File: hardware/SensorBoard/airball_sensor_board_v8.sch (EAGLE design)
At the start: 61 parts, among them IC1 CP2102, J2 USB Female Type C Connector, T1 BC846, T2 BC846, U1 BQ24075, U2 BQ27441-G1, U3 BMP388, U4 ESP-WROOM-32, U7 SP0503BAHT

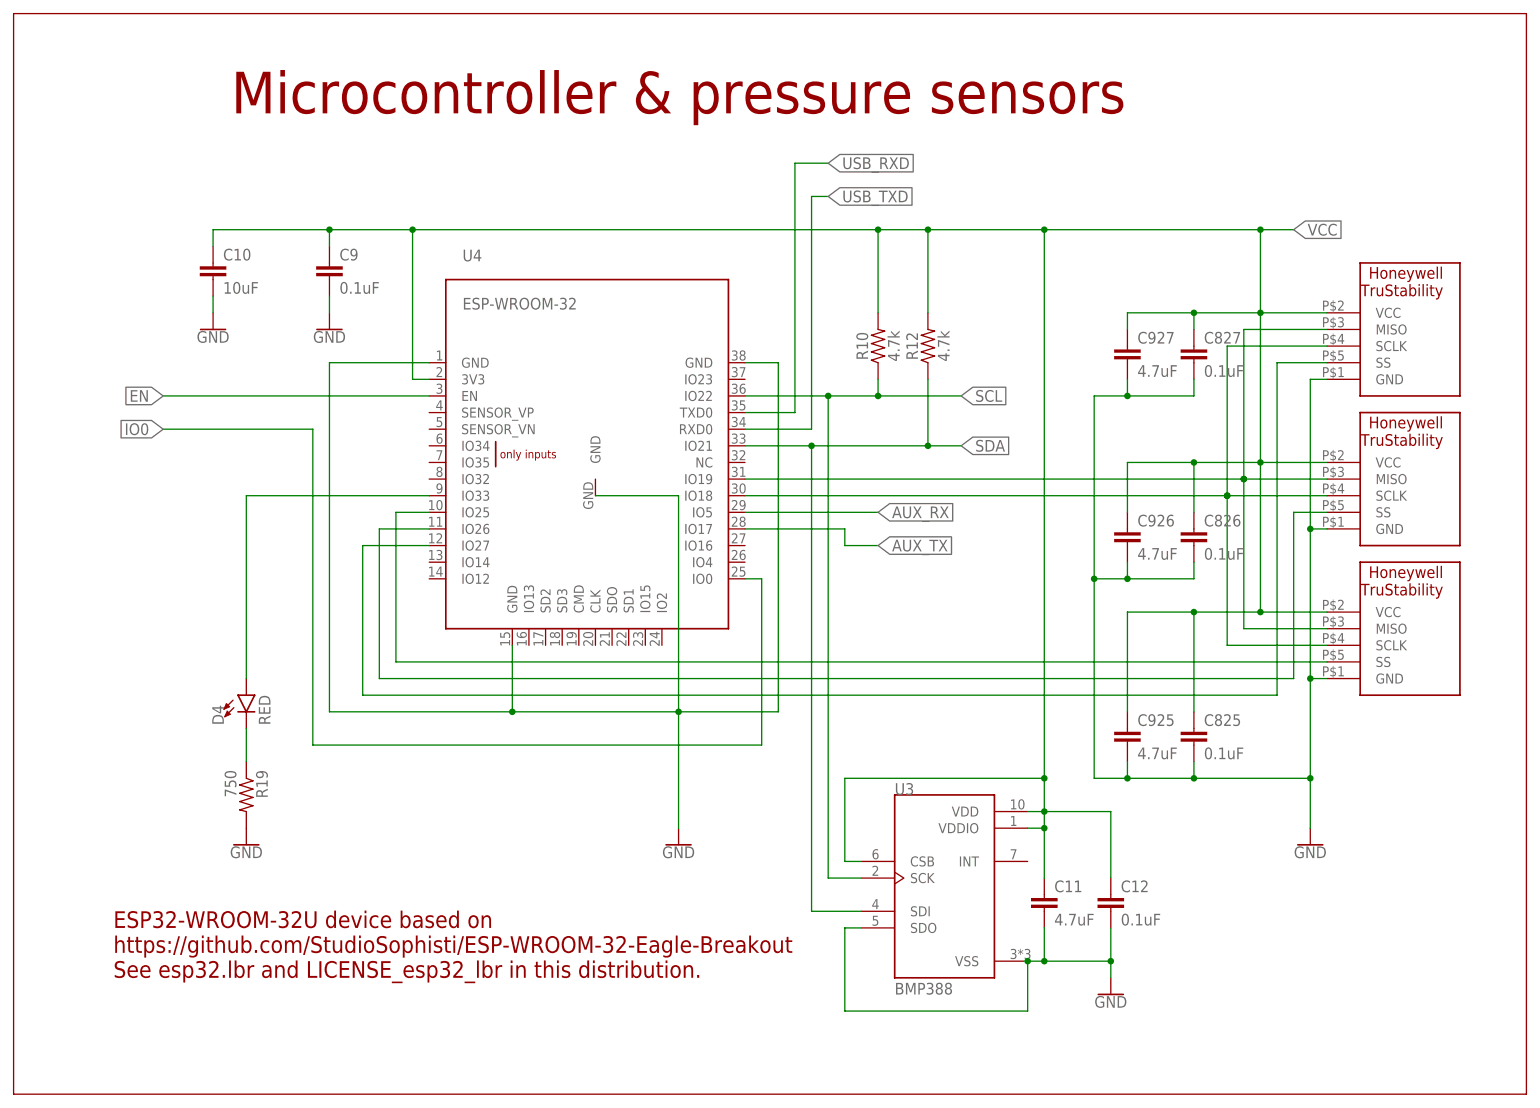
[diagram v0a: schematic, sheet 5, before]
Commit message: Next rev of sensor board v8
Moved pressure sensors to more accessible location; added a pullup and
capacitor for one of the ESP32 pins for USB access; changed pressure
sensor to the newer BMP390; changed pressure sensor pads to support
either SMD or thru-hole variants; cleaned up the locations of the
barometer and its mounting holes.
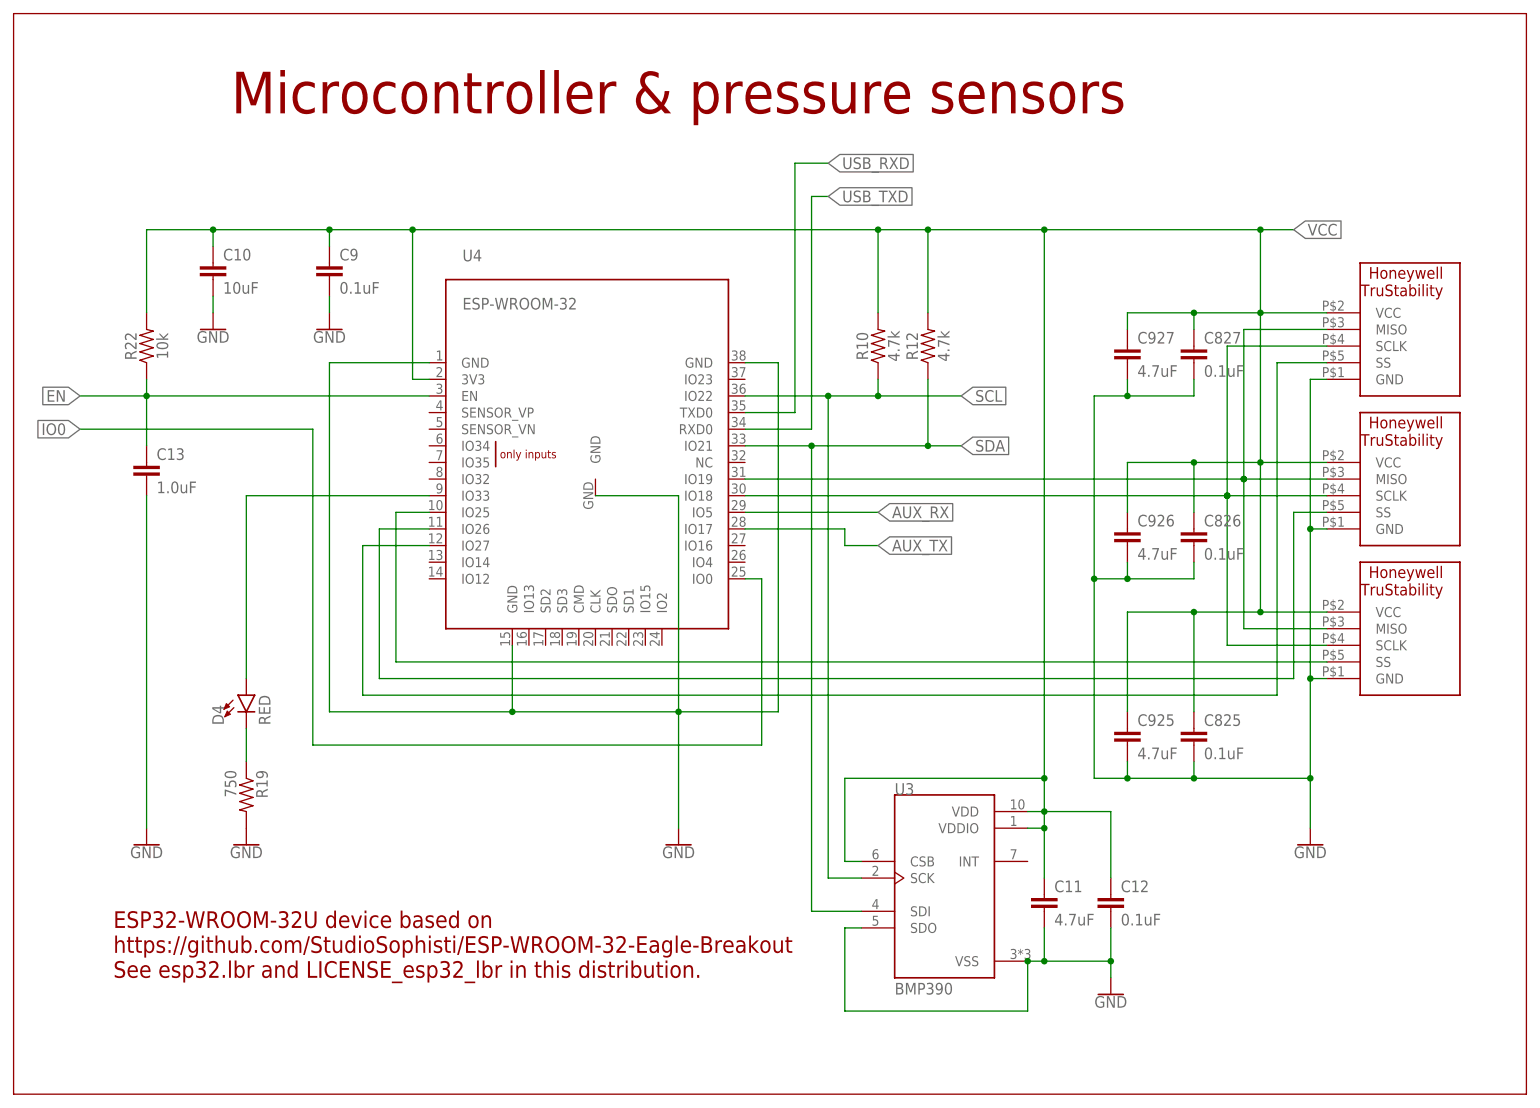
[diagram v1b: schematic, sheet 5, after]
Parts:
- added C13: 1.0uF, SparkFun-Capacitors:1.0UF-0603-16V-10%
- added R22: 10k, SparkFun-Resistors:10KOHM-0603-1/10W-1%
- U3: value BMP388 -> BMP390; device BMP388:BMP388 -> BMP388:BMP390
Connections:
- net EN: now also C13.1, R22.1
- net GND: now also C13.2; no longer U1.!CE!
- net SYSOFF: now also U1.!CE!
- net VCC: now also R22.2
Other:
- note added: "D1 = Charging D2 = USB power available D3 = System powered on With SYSOFF high, the BQ24075 pulls down its !CHG pin even though it is not actually charging the battery!! We tie SYSOFF to !CHG, so that the "Charging" LED tells the truth."
- note removed: "D1 = Charging D2 = USB power available D3 = System powered on"
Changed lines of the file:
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@@
 <part name="J1" library="SparkFun-Connectors" deviceset="CONN_04" device="PTH"/>
 <part name="GND21" library="SparkFun-Aesthetics" deviceset="GND" device=""/>
-<part name="U3" library="BMP388" deviceset="BMP388" device=""/>
+<part name="U3" library="BMP388" deviceset="BMP390" device=""/>
 <part name="U$927" library="airball" deviceset="HONEYWELL_HSC_SMT" device=""/>
 <part name="U$926" library="airball" deviceset="HONEYWELL_HSC_SMT" device=""/>
@@
 <part name="GND13" library="SparkFun-Aesthetics" deviceset="GND" device=""/>
 <part name="U$3" library="airball" deviceset="NKK_SPDT_SS312SAH4-R" device=""/>
+<part name="R22" library="SparkFun-Resistors" deviceset="10KOHM" device="-0603-1/10W-1%" value="10k"/>
+<part name="C13" library="SparkFun-Capacitors" deviceset="1.0UF" device="-0603-16V-10%" value="1.0uF"/>
+<part name="GND29" library="SparkFun-PowerSymbols" deviceset="GND" device=""/>
 </parts>
 <sheets>
@@
 Current Sense
 Resistor</text>
-<text x="129.54" y="15.24" size="1.778" layer="94">D1 = Charging
+<text x="121.92" y="0" size="1.778" layer="94">D1 = Charging
 D2 = USB power available
-D3 = System powered on</text>
+D3 = System powered on
+With SYSOFF high, the BQ24075 pulls
+down its !CHG pin even though it is
+not actually charging the battery!!
+We tie SYSOFF to !CHG, so that the
+"Charging" LED tells the truth.</text>
 <wire x1="59.69" y1="47.244" x2="52.07" y2="47.244" width="0.1524" layer="94"/>
 <wire x1="54.61" y1="48.514" x2="52.07" y2="47.244" width="0.1524" layer="94"/>
@@
 <wire x1="45.974" y1="92.71" x2="44.704" y2="95.25" width="0.1524" layer="94"/>
 <wire x1="44.704" y1="95.25" x2="43.434" y2="92.71" width="0.1524" layer="94"/>
-<wire x1="0" y1="129.54" x2="0" y2="0" width="0.1524" layer="94"/>
-<wire x1="0" y1="0" x2="256.54" y2="0" width="0.1524" layer="94"/>
-<wire x1="256.54" y1="0" x2="256.54" y2="129.54" width="0.1524" layer="94"/>
+<wire x1="0" y1="129.54" x2="0" y2="-2.54" width="0.1524" layer="94"/>
+<wire x1="0" y1="-2.54" x2="256.54" y2="-2.54" width="0.1524" layer="94"/>
+<wire x1="256.54" y1="-2.54" x2="256.54" y2="129.54" width="0.1524" layer="94"/>
 <wire x1="256.54" y1="129.54" x2="0" y2="129.54" width="0.1524" layer="94"/>
 <wire x1="118.11" y1="52.324" x2="125.73" y2="52.324" width="0.1524" layer="94"/>
@@
 </segment>
 <segment>
-<pinref part="U1" gate="G$1" pin="!CE!"/>
-<wire x1="109.22" y1="35.56" x2="114.3" y2="35.56" width="0.1524" layer="91"/>
-<wire x1="114.3" y1="35.56" x2="114.3" y2="10.16" width="0.1524" layer="91"/>
+<wire x1="114.3" y1="43.18" x2="114.3" y2="10.16" width="0.1524" layer="91"/>
 <pinref part="GND14" gate="1" pin="GND"/>
 <pinref part="U1" gate="G$1" pin="EN2"/>
 <wire x1="109.22" y1="43.18" x2="114.3" y2="43.18" width="0.1524" layer="91"/>
-<wire x1="114.3" y1="43.18" x2="114.3" y2="35.56" width="0.1524" layer="91"/>
-<junction x="114.3" y="35.56"/>
 </segment>
 <segment>
@@
 <wire x1="111.76" y1="38.1" x2="111.76" y2="60.96" width="0.1524" layer="91"/>
 <wire x1="111.76" y1="60.96" x2="226.06" y2="60.96" width="0.1524" layer="91"/>
+<pinref part="U1" gate="G$1" pin="!CE!"/>
+<wire x1="111.76" y1="38.1" x2="111.76" y2="35.56" width="0.1524" layer="91"/>
+<wire x1="111.76" y1="35.56" x2="109.22" y2="35.56" width="0.1524" layer="91"/>
+<junction x="111.76" y="38.1"/>
 </segment>
 </net>
@@
 <attribute name="NAME" x="169.164" y="30.861" size="1.778" layer="95" font="vector"/>
 <attribute name="VALUE" x="169.164" y="25.781" size="1.778" layer="96" font="vector"/>
+</instance>
+<instance part="R22" gate="G$1" x="20.32" y="114.3" smashed="yes" rot="R90">
+<attribute name="NAME" x="18.796" y="114.3" size="1.778" layer="95" font="vector" rot="R90" align="bottom-center"/>
+<attribute name="VALUE" x="21.844" y="114.3" size="1.778" layer="96" font="vector" rot="R90" align="top-center"/>
+</instance>
+<instance part="C13" gate="G$1" x="20.32" y="93.98" smashed="yes">
+<attribute name="NAME" x="21.844" y="96.901" size="1.778" layer="95" font="vector"/>
+<attribute name="VALUE" x="21.844" y="91.821" size="1.778" layer="96" font="vector"/>
+</instance>
+<instance part="GND29" gate="1" x="20.32" y="38.1" smashed="yes">
+<attribute name="VALUE" x="20.32" y="37.846" size="1.778" layer="96" align="top-center"/>
 </instance>
 </instances>
@@
 <pinref part="R19" gate="G$1" pin="2"/>
 <pinref part="GND32" gate="1" pin="GND"/>
+</segment>
+<segment>
+<pinref part="C13" gate="G$1" pin="2"/>
+<pinref part="GND29" gate="1" pin="GND"/>
+<wire x1="20.32" y1="91.44" x2="20.32" y2="40.64" width="0.1524" layer="91"/>
 </segment>
 </net>
@@
 <wire x1="127" y1="48.26" x2="157.48" y2="48.26" width="0.1524" layer="91"/>
 <junction x="157.48" y="48.26"/>
+<pinref part="R22" gate="G$1" pin="2"/>
+<wire x1="20.32" y1="119.38" x2="20.32" y2="132.08" width="0.1524" layer="91"/>
+<wire x1="20.32" y1="132.08" x2="30.48" y2="132.08" width="0.1524" layer="91"/>
+<junction x="30.48" y="132.08"/>
 </segment>
 </net>
@@
 <segment>
 <pinref part="U4" gate="G$1" pin="EN"/>
-<wire x1="63.5" y1="106.68" x2="22.86" y2="106.68" width="0.1524" layer="91"/>
-<label x="22.86" y="106.68" size="1.778" layer="95" rot="MR0" xref="yes"/>
+<wire x1="63.5" y1="106.68" x2="20.32" y2="106.68" width="0.1524" layer="91"/>
+<label x="10.16" y="106.68" size="1.778" layer="95" rot="MR0" xref="yes"/>
+<pinref part="R22" gate="G$1" pin="1"/>
+<wire x1="20.32" y1="106.68" x2="10.16" y2="106.68" width="0.1524" layer="91"/>
+<wire x1="20.32" y1="109.22" x2="20.32" y2="106.68" width="0.1524" layer="91"/>
+<junction x="20.32" y="106.68"/>
+<pinref part="C13" gate="G$1" pin="1"/>
+<wire x1="20.32" y1="106.68" x2="20.32" y2="99.06" width="0.1524" layer="91"/>
 </segment>
 </net>
@@
 <pinref part="U4" gate="G$1" pin="IO0"/>
 <wire x1="114.3" y1="78.74" x2="111.76" y2="78.74" width="0.1524" layer="91"/>
-<wire x1="45.72" y1="101.6" x2="22.86" y2="101.6" width="0.1524" layer="91"/>
-<label x="22.86" y="101.6" size="1.778" layer="95" rot="MR0" xref="yes"/>
-</segment>
-</net>
+<wire x1="45.72" y1="101.6" x2="10.16" y2="101.6" width="0.1524" layer="91"/>
+<label x="10.16" y="101.6" size="1.778" layer="95" rot="MR0" xref="yes"/>
+</segment>
+</net>

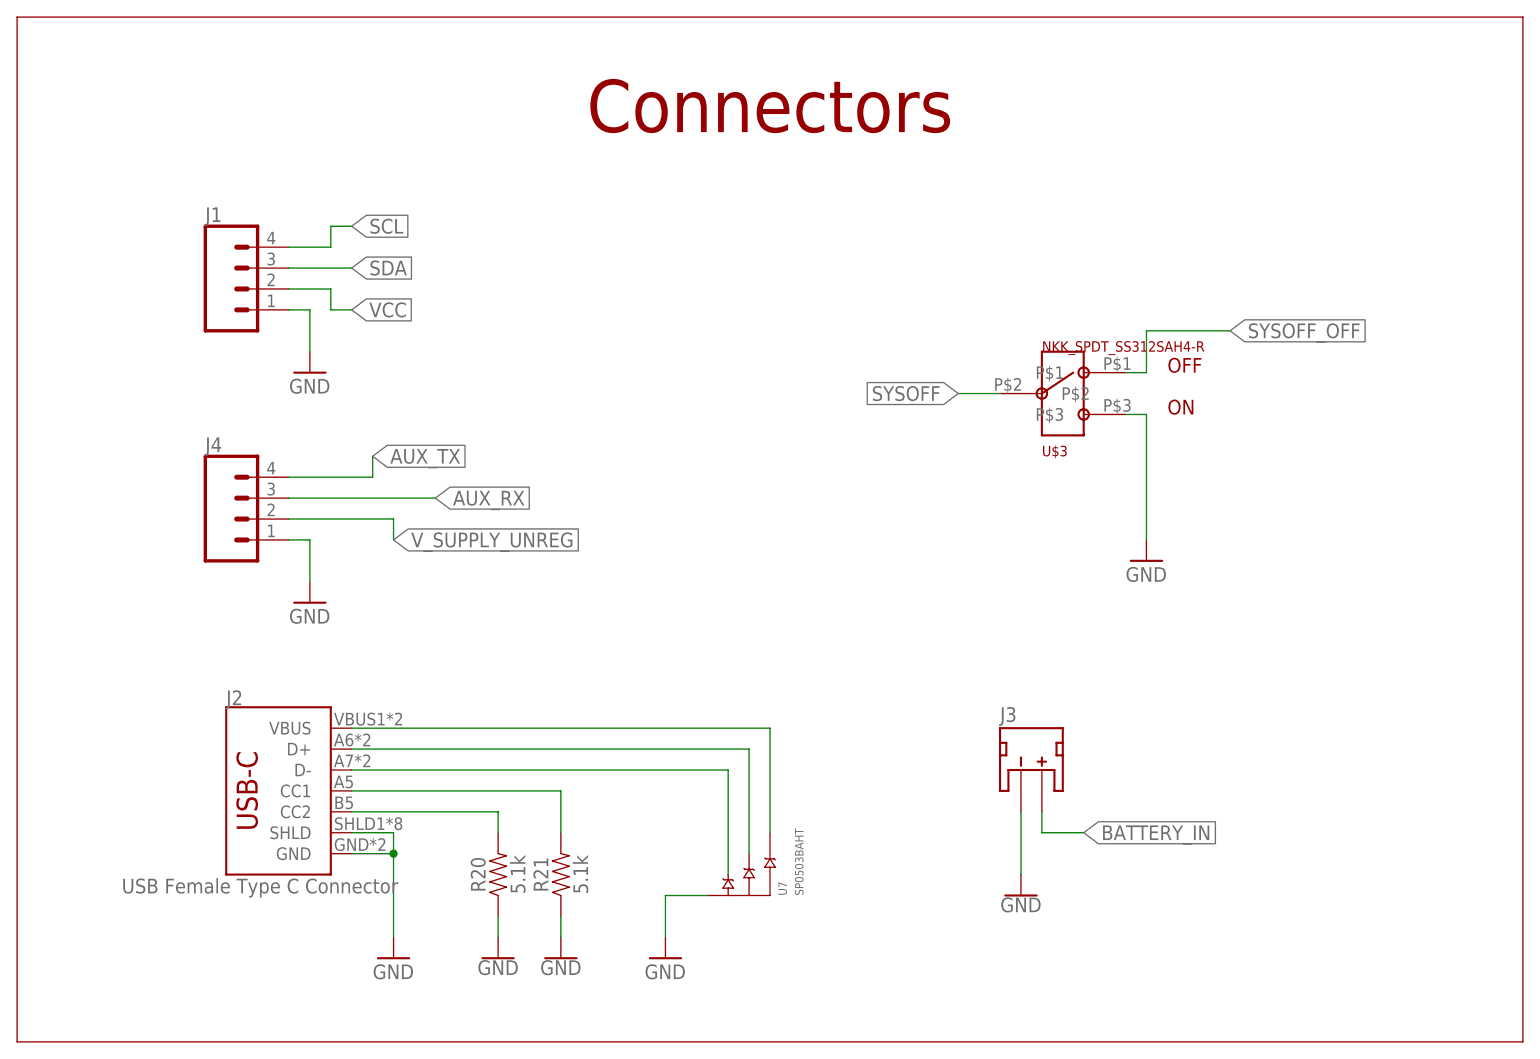
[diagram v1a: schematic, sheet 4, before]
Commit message: Changed to Molex USB-C connector
Switched to a more readily available Molex USB-C connector.
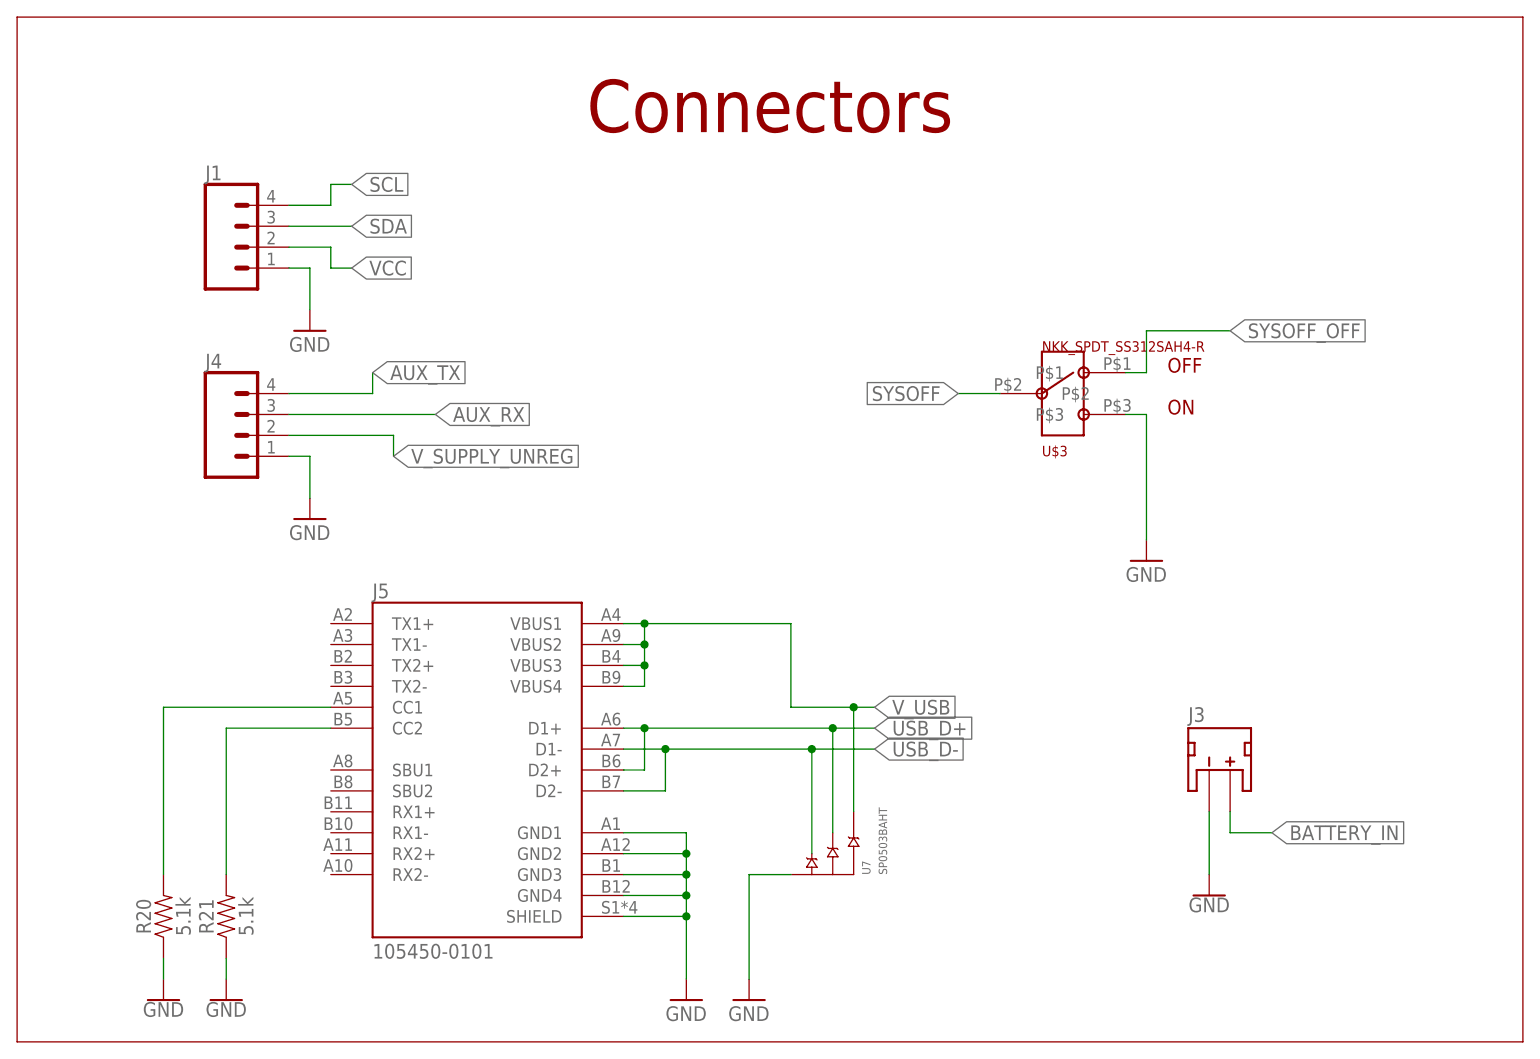
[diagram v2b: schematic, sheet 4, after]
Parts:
- removed J2: USB Female Type C Connector, SparkFun-Connectors:USB_C
- added J5: 105450-0101, 105450-0101:105450-0101
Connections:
- removed net N$10: J2.CC2, R20.2
- removed net N$13: J2.CC1, R21.2
- new net USB_CC1: J5.CC1, R20.2
- new net USB_CC2: J5.CC2, R21.2
- net GND: now also J5.GND1, J5.GND2, J5.GND3, J5.GND4, J5.SHIELD; no longer J2.GND, J2.SHLD
- net USB_D+: now also J5.D1+, J5.D2+; no longer J2.D+
- net USB_D-: now also J5.D1-, J5.D2-; no longer J2.D-
- net V_USB: now also J5.VBUS1, J5.VBUS2, J5.VBUS3, J5.VBUS4; no longer J2.VBUS
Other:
- moved on the sheet: J1, J3, J4, R20, R21, U7
